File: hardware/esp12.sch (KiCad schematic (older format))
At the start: 0 parts

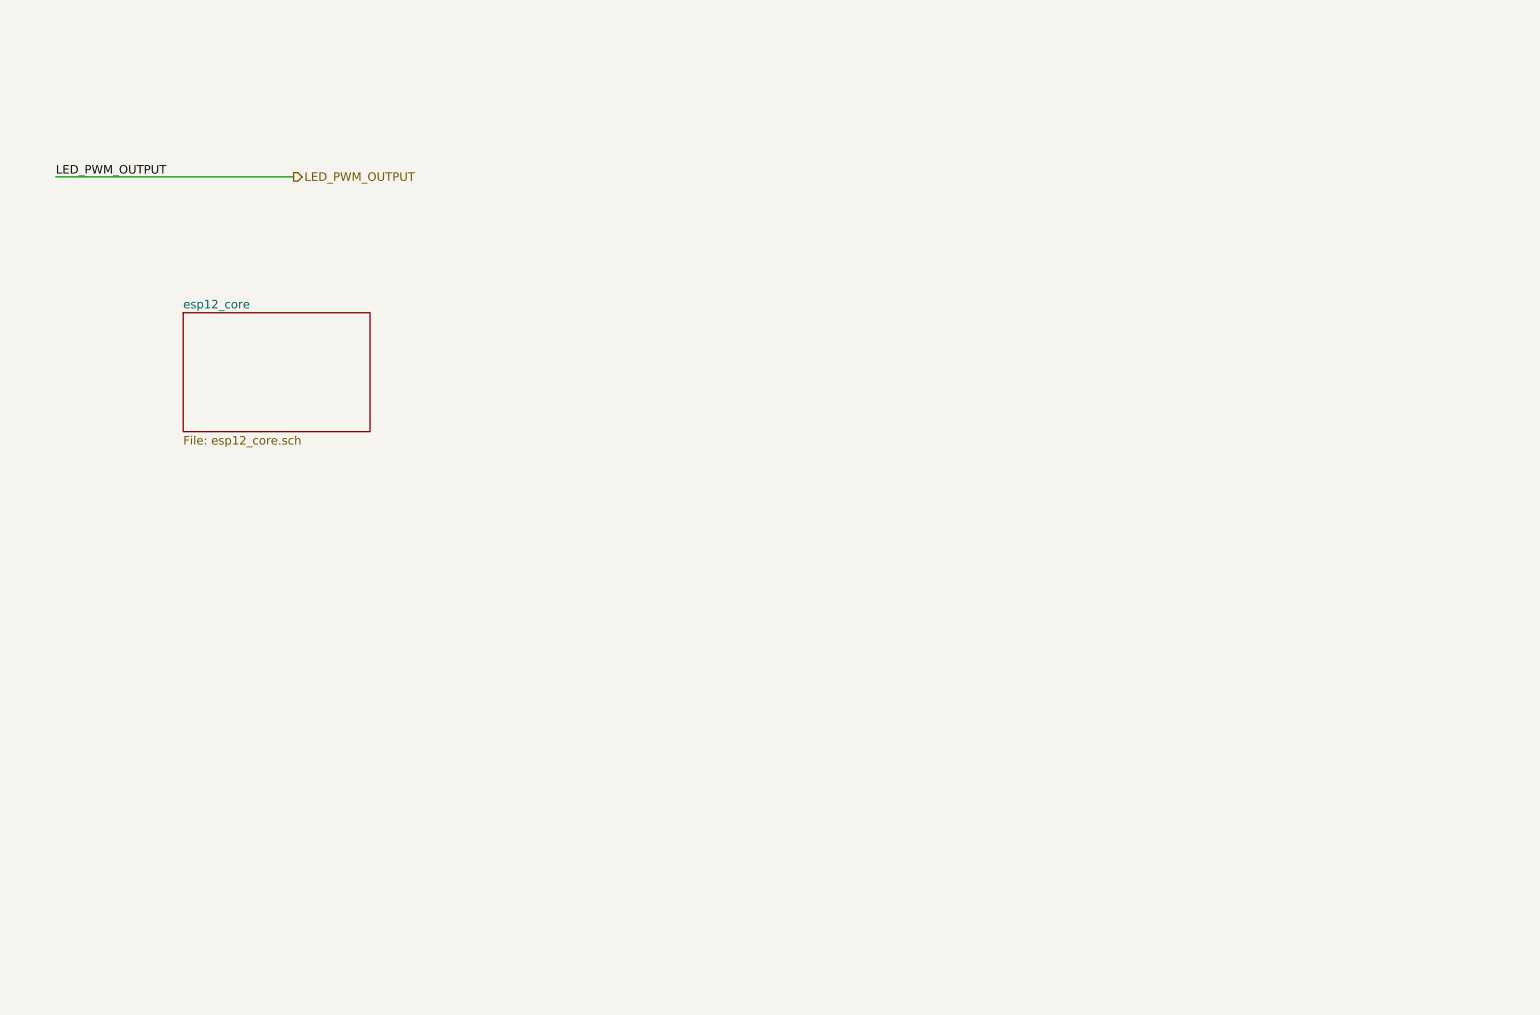
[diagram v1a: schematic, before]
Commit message: update WS2812\,
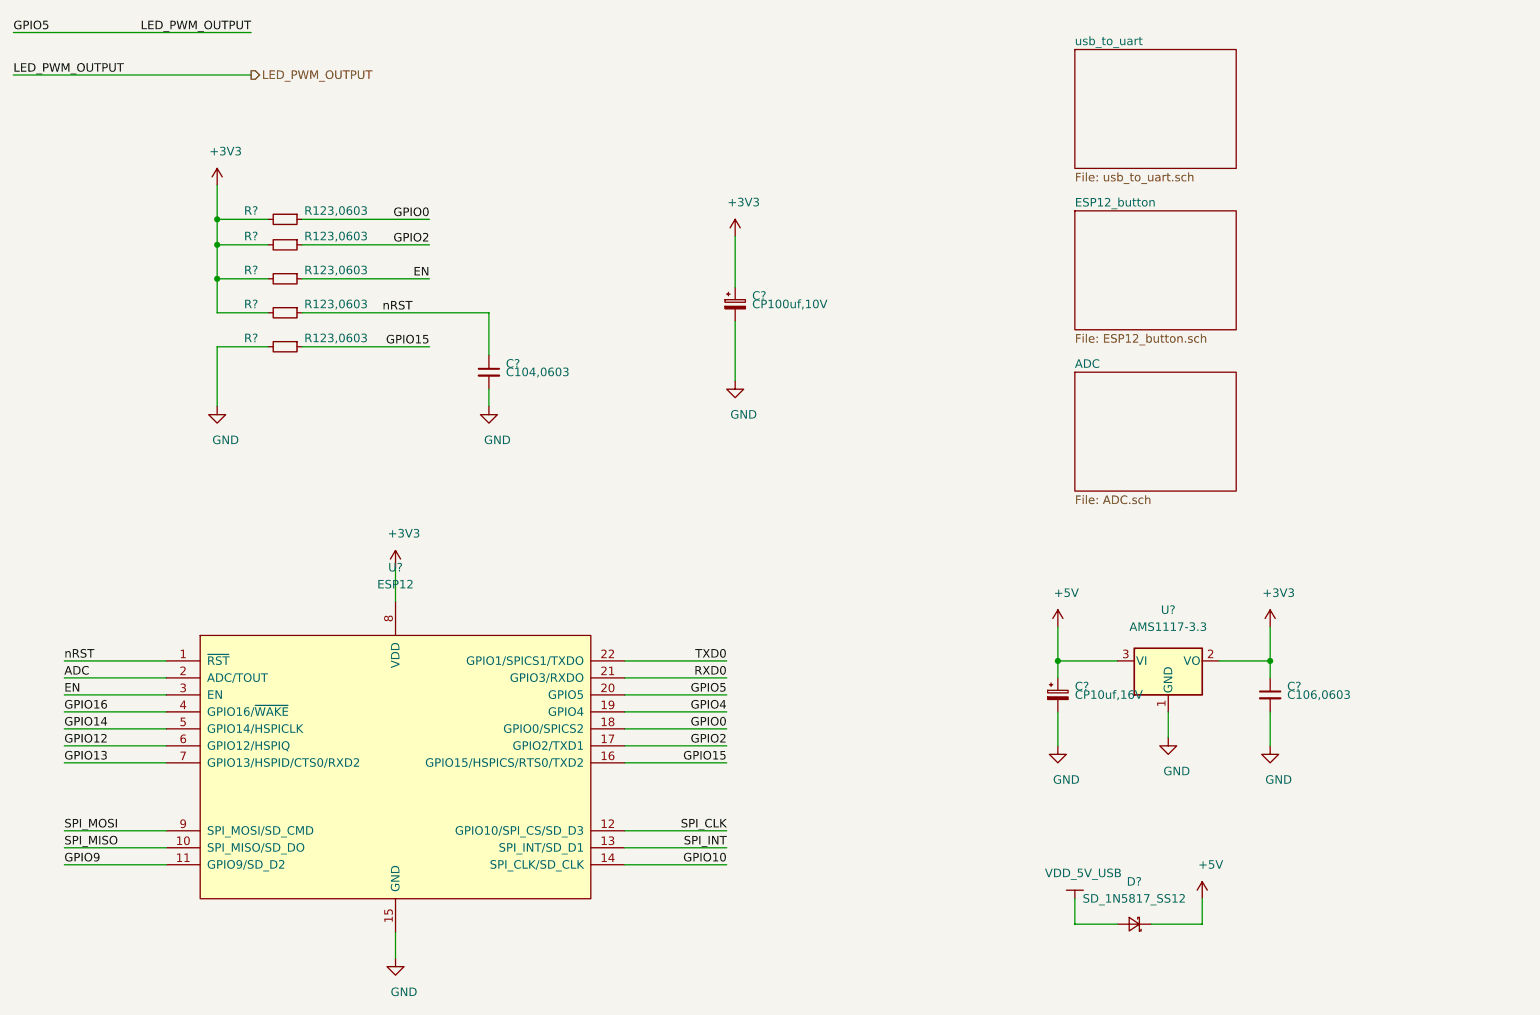
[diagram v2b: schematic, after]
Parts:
- added C?: C104,0603, Capacitor_SMD:C_0603_1608Metric_Pad1.05x0.95mm_HandSolder, symbol taobao-c:C104,0603
- added C?: CP10uf,16V, Capacitor_SMD:CP_Elec_4x5.3, symbol taobao-cp:CP10uf,16V
- added C?: C106,0603, Capacitor_SMD:C_0603_1608Metric_Pad1.05x0.95mm_HandSolder, symbol taobao-c:C106,0603
- added C?: CP100uf,10V, Capacitor_SMD:CP_Elec_6.3x5.3, symbol taobao-cp:CP100uf,10V
- added D?: SD_1N5817_SS12, footprint-lib:SS12,do214ac, symbol taobao-sd:SD_1N5817_SS12
- added R? (x5): R123,0603, Resistor_SMD:R_0603_1608Metric_Pad1.05x0.95mm_HandSolder, symbol taobao-r:R123,0603
- added U?: AMS1117-3.3, footprint-lib:AMS1117_SOT-223, symbol taobao-components:AMS1117-3.3
- added U?: ESP12, footprint-lib:ESP-12, symbol taobao-components:ESP12
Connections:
- net LED_PWM_OUTPUT: now also U?.20 (GPIO5)
- new net +3V3: C?.1, C?.1, R?.2, R?.2, R?.2, R?.2, U?.2 (VO), U?.8 (VDD)
- new net +5V: C?.1, D?.1 (K), U?.3 (VI)
- new net ADC: U?.2 (ADC/TOUT)
- new net EN: R?.1, U?.3 (EN)
- new net GND: C?.2, C?.2, C?.2, C?.2, R?.2, U?.1 (GND), U?.15 (GND)
- new net GPIO0: R?.1, U?.18 (GPIO0/SPICS2)
- new net GPIO10: U?.14 (SPI_CLK/SD_CLK)
- new net GPIO12: U?.6 (GPIO12/HSPIQ)
- new net GPIO13: U?.7 (GPIO13/HSPID/CTS0/RXD2)
- new net GPIO14: U?.5 (GPIO14/HSPICLK)
- new net GPIO15: R?.1, U?.16 (GPIO15/HSPICS/RTS0/TXD2)
- new net GPIO16: U?.4 (GPIO16/~WAKE~)
- new net GPIO2: R?.1, U?.17 (GPIO2/TXD1)
- new net GPIO4: U?.19 (GPIO4)
- new net GPIO9: U?.11 (GPIO9/SD_D2)
- new net RXD0: U?.21 (GPIO3/RXDO)
- new net SPI_CLK: U?.12 (GPIO10/SPI_CS/SD_D3)
- new net SPI_INT: U?.13 (SPI_INT/SD_D1)
- new net SPI_MISO: U?.10 (SPI_MISO/SD_DO)
- new net SPI_MOSI: U?.9 (SPI_MOSI/SD_CMD)
- new net TXD0: U?.22 (GPIO1/SPICS1/TXDO)
- new net VDD_5V_USB: D?.2 (A)
- new net nRST: C?.1, R?.1, U?.1 (~RST~)

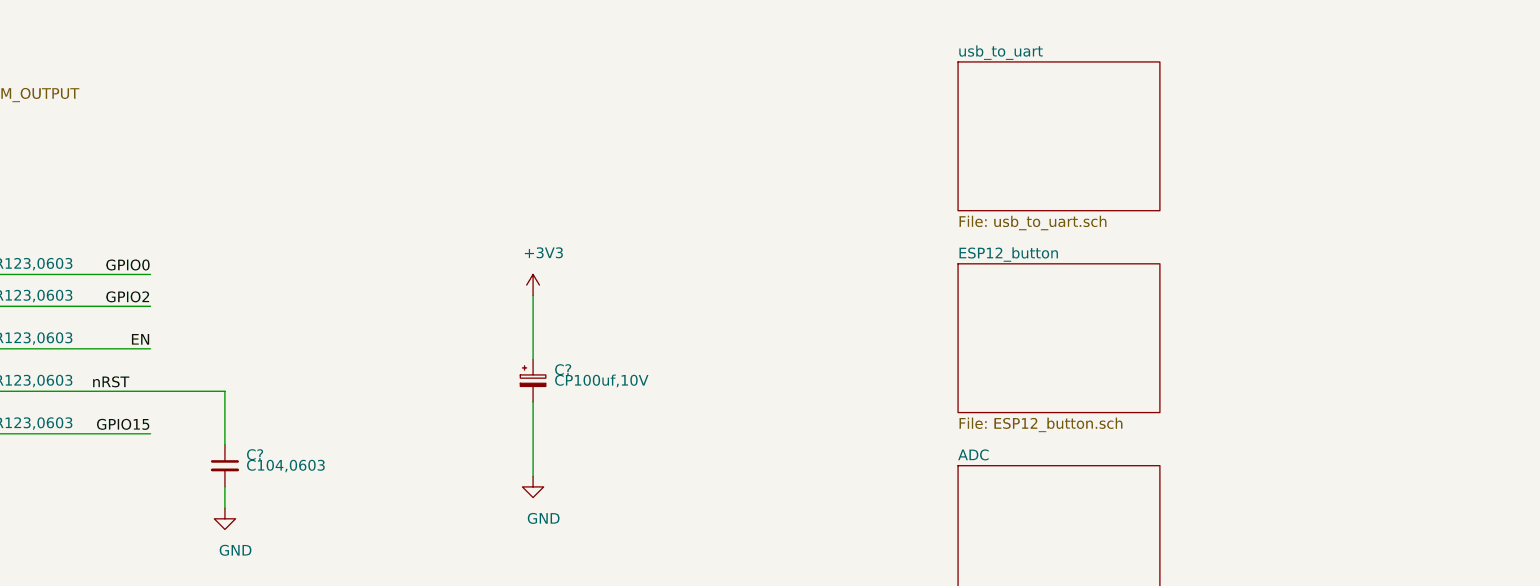
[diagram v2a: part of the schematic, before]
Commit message: update WS2812\,
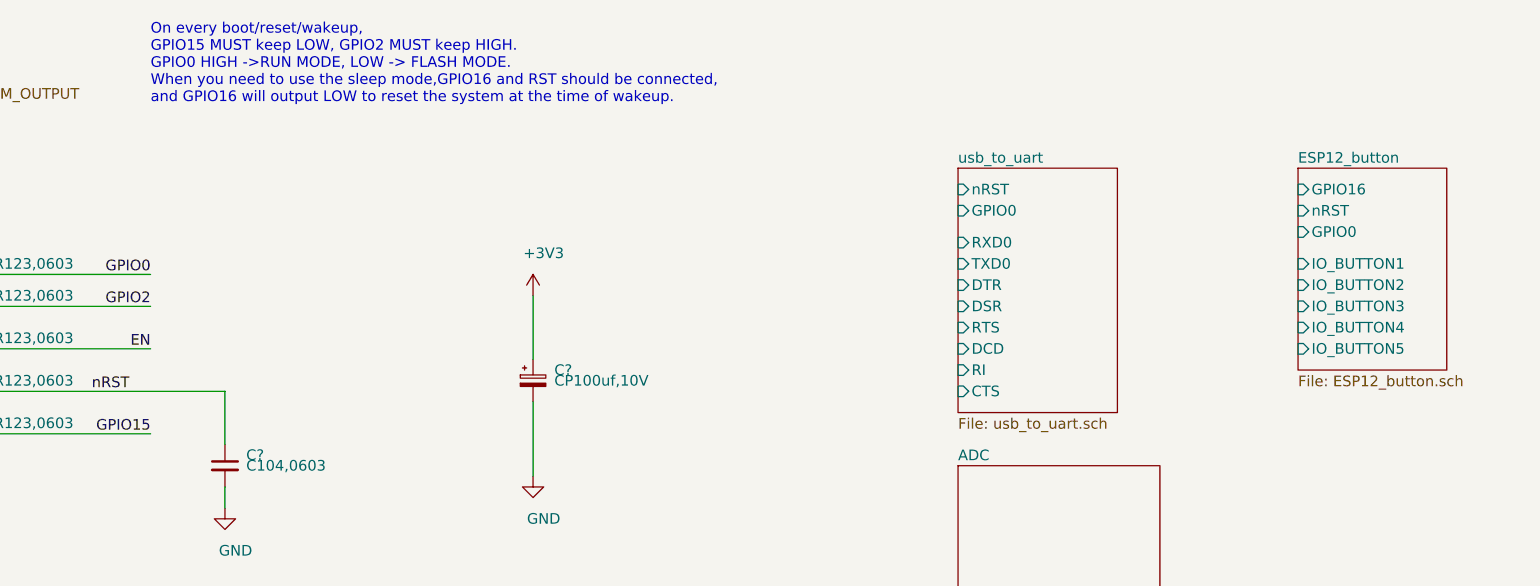
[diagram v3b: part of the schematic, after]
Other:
- note added: "On every boot/reset/wakeup,\nGPIO15 MUST keep LOW, GPIO2 MUST keep HIGH.\nGPIO0 HIGH ->RUN MODE, LOW -> FLASH MODE.\nWhen you need to use the sleep mode,GPIO16 and RST should be connected,\nand GPIO16 will output LOW to reset the system at the time of wakeup."
